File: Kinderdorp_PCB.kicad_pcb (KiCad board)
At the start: 2 copper layers, 39 parts, among them J1 Conn_01x08, Q1 2N7002_C306856, U2 AMS1117-3.3_C347222, U5 ESP32-C3-WROOM-02-N4(4MB)

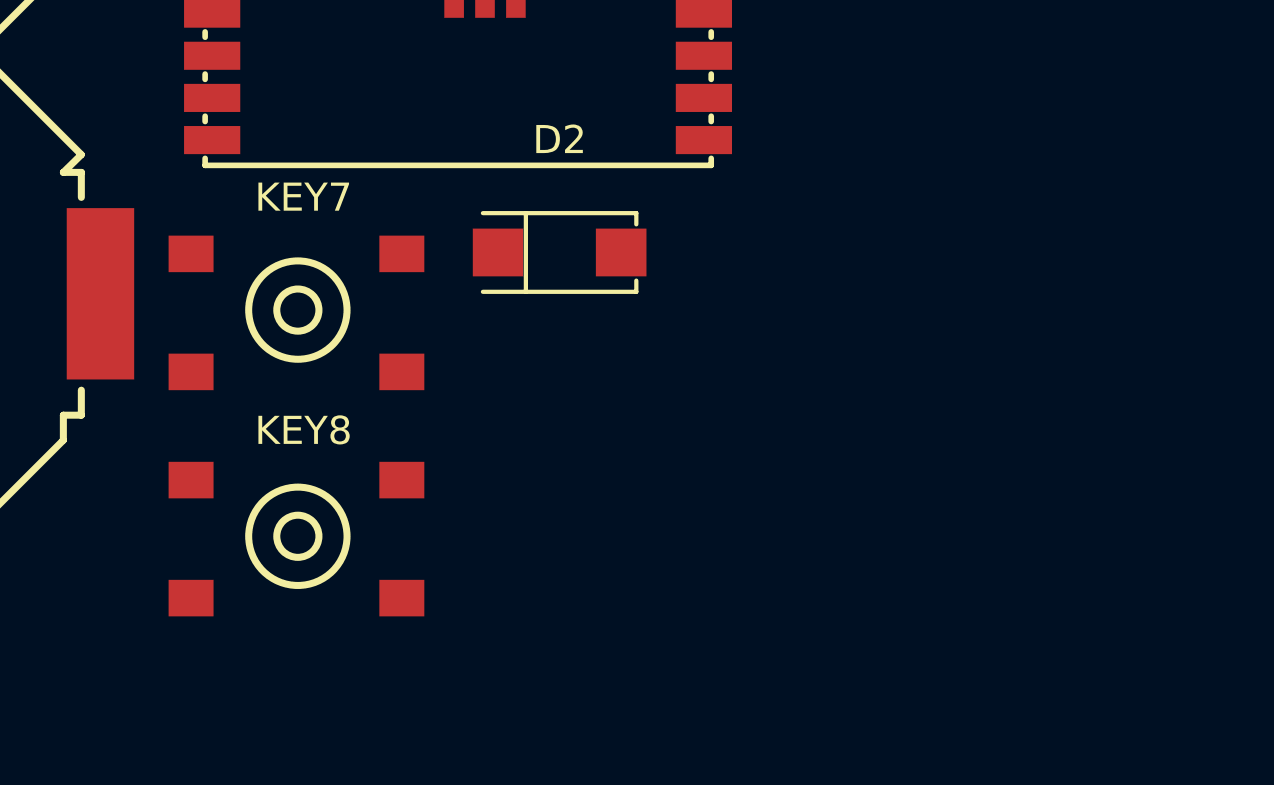
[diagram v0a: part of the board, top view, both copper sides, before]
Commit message: updated all 3d models
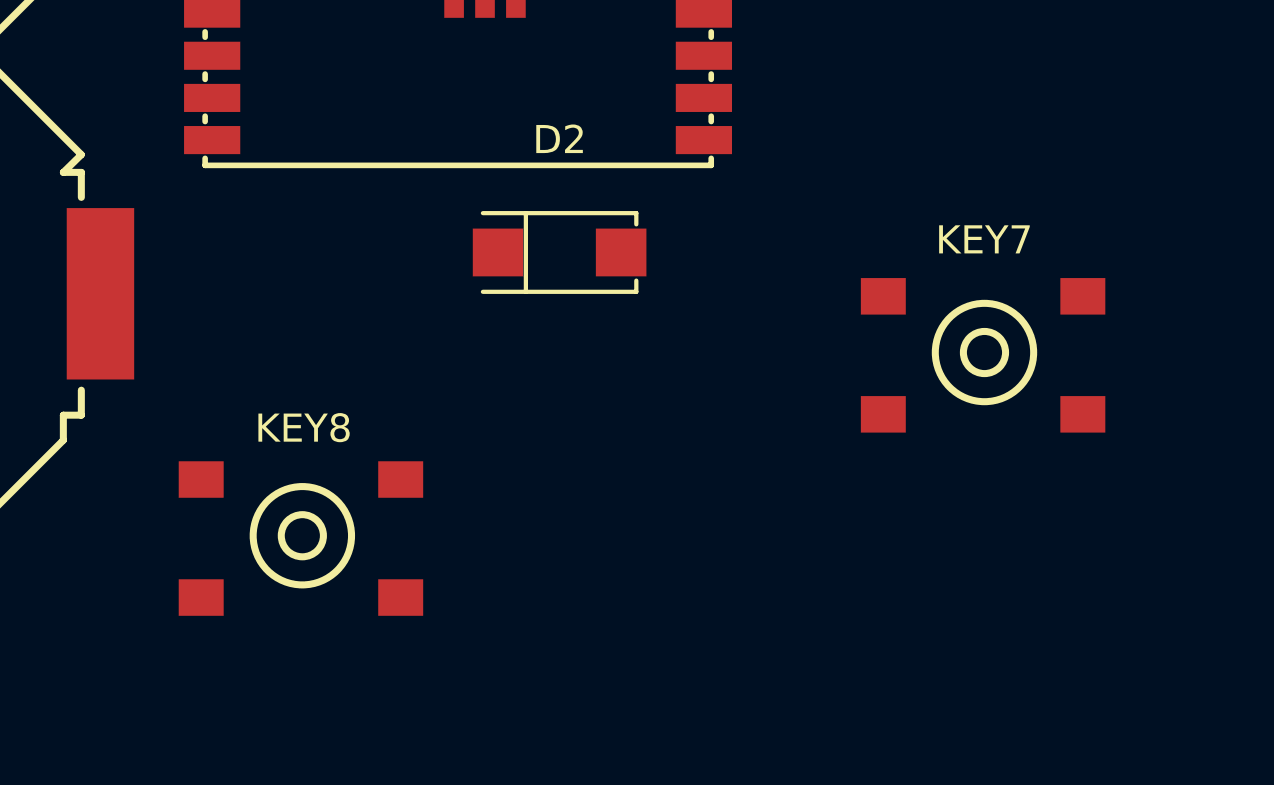
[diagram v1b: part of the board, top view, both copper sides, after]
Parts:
- moved KEY7 24.3 mm to (107.5, 84.6)
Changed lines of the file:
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@@
 		)
 		(embedded_fonts no)
-		(model "${EASYEDA2KICAD}/easyeda2kicad.3dshapes/LED-SMD_4P-L5.0-W5.0-BL_TC5050RGB.wrl"
+		(model "${KIPRJMOD}/packages3D/LED-SMD_4P-L5.0-W5.0-BL_TC5050RGB.step"
 			(offset
 				(xyz 0 -0 -0)
@@
 		(model "${KICAD9_3DMODEL_DIR}/OptoDevice.3dshapes/R_LDR_5.1x4.3mm_P3.4mm_Vertical.wrl"
 			(offset
-				(xyz 0 0 0)
+				(xyz 0 0 -2.2)
 			)
 			(scale
@@
 			)
 			(rotate
-				(xyz 0 0 0)
+				(xyz -0 -0 -0)
 			)
 		)
@@
 		)
 		(embedded_fonts no)
-		(model "${EASYEDA2KICAD}/easyeda2kicad.3dshapes/SOT-223-4P_L6.5-W3.5-H1.6-LS7.0-P2.30.wrl"
+		(model "${KIPRJMOD}/packages3D/SOT-223-4P_L6.5-W3.5-H1.6-LS7.0-P2.30.step"
 			(offset
-				(xyz -941.76 660.4 -0)
+				(xyz 0 0 -0)
 			)
 			(scale
@@
 			)
 			(rotate
-				(xyz 0 0 180)
+				(xyz -0 -0 180)
 			)
 		)
@@
 		)
 		(embedded_fonts no)
-		(model "${EASYEDA2KICAD}/easyeda2kicad.3dshapes/LED-SMD_4P-L5.0-W5.0-BL_TC5050RGB.wrl"
+		(model "${KIPRJMOD}/packages3D/LED-SMD_4P-L5.0-W5.0-BL_TC5050RGB.step"
 			(offset
 				(xyz 0 -0 -0)
@@
 		)
 		(embedded_fonts no)
-		(model "${EASYEDA2KICAD}/easyeda2kicad.3dshapes/LED-SMD_4P-L5.0-W5.0-BL_TC5050RGB.wrl"
+		(model "${KIPRJMOD}/packages3D/LED-SMD_4P-L5.0-W5.0-BL_TC5050RGB.step"
 			(offset
 				(xyz 0 -0 -0)
@@
 		)
 		(embedded_fonts no)
-		(model "${EASYEDA2KICAD}/easyeda2kicad.3dshapes/LED-SMD_4P-L5.0-W5.0-BL_TC5050RGB.wrl"
+		(model "${KIPRJMOD}/packages3D/LED-SMD_4P-L5.0-W5.0-BL_TC5050RGB.step"
 			(offset
 				(xyz 0 -0 -0)
@@
 	(footprint "easyeda2kicad:KEY-SMD_4P-L6.2-W6.2-P4.50-LS9.0"
 		(layer "F.Cu")
-		(at 83.225 83.08)
+		(at 107.45 84.6)
 		(property "Reference" "KEY7"
 			(at 0 -4 0)
@@
 			(at 0 6.25 0)
 			(layer "F.Fab")
+			(hide yes)
 			(effects
 				(font
@@
 		(attr smd)
 		(fp_circle
-			(center -0.2 0)
-			(end 0.55 0)
+			(center 0.01 -0.01)
+			(end 0.76 -0.01)
 			(stroke
 				(width 0.25)
@@
 		)
 		(fp_circle
-			(center -0.2 0)
-			(end 1.55 0)
+			(center 0.01 -0.01)
+			(end 1.76 -0.01)
 			(stroke
 				(width 0.25)
@@
 		)
 		(fp_rect
-			(start -5 -3.25)
-			(end 4.5 3.25)
+			(start -4.59 -2.93)
+			(end 4.51 3.07)
 			(stroke
 				(width 0.05)
@@
 		)
 		(fp_circle
-			(center -4.5 -2.85)
-			(end -4.47 -2.85)
+			(center -4.09 -2.86)
+			(end -4.06 -2.86)
 			(stroke
 				(width 0.06)
@@
 		)
 		(fp_text user "${REFERENCE}"
-			(at 0 0.25 0)
+			(at 0.41 0.24 0)
 			(layer "F.Fab")
 			(effects
@@
 		)
 		(pad "1" smd rect
-			(at -4 -2 180)
+			(at -3.59 -2.01 180)
 			(size 1.6 1.3)
 			(layers "F.Cu" "F.Mask" "F.Paste")
@@
 		)
 		(pad "2" smd rect
-			(at 3.5 -2 180)
+			(at -3.59 2.19 180)
 			(size 1.6 1.3)
 			(layers "F.Cu" "F.Mask" "F.Paste")
@@
 		)
 		(pad "3" smd rect
-			(at -4 2.2 180)
+			(at 3.51 -2.01 180)
 			(size 1.6 1.3)
 			(layers "F.Cu" "F.Mask" "F.Paste")
@@
 		)
 		(pad "4" smd rect
-			(at 3.5 2.2 180)
+			(at 3.51 2.19 180)
 			(size 1.6 1.3)
 			(layers "F.Cu" "F.Mask" "F.Paste")
@@
 		)
 		(embedded_fonts no)
-		(model "${EASYEDA2KICAD}/easyeda2kicad.3dshapes/KEY-SMD_4P-L6.2-W6.2-H5.0-LS9.0-P4.5.wrl"
+		(model "${KIPRJMOD}/packages3D/Tactile_SMD_5x5mm.STEP"
 			(offset
 				(xyz 0 -0 -0)
 			)
 			(scale
-				(xyz 1 1 1)
+				(xyz 1.1 1.1 1)
 			)
 			(rotate
-				(xyz 0 0 0)
+				(xyz -0 -0 -0)
 			)
 		)
@@
 		)
 		(embedded_fonts no)
-		(model "${EASYEDA2KICAD}/easyeda2kicad.3dshapes/LED-SMD_4P-L5.0-W5.0-BL_TC5050RGB.wrl"
+		(model "${KIPRJMOD}/packages3D/LED-SMD_4P-L5.0-W5.0-BL_TC5050RGB.step"
 			(offset
 				(xyz 0 -0 -0)
@@
 		)
 		(embedded_fonts no)
+		(model "${KIPRJMOD}/packages3D/Buzzer.STEP"
+			(offset
+				(xyz 0 0 0)
+			)
+			(scale
+				(xyz 1 1 1)
+			)
+			(rotate
+				(xyz -90 -0 -90)
+			)
+		)
 	)
 	(footprint "easyeda2kicad:SOT-23-3_L2.9-W1.3-P1.90-LS2.4-BR"
@@
 		)
 		(embedded_fonts no)
-		(model "${EASYEDA2KICAD}/easyeda2kicad.3dshapes/SOT-23-3P_L2.9-W1.3-H1.0-LS2.4-P0.95.wrl"
+		(model "${KIPRJMOD}/packages3D/SOT-23.step"
 			(offset
-				(xyz -861.57 843.28 -0)
+				(xyz 0 0 -0)
 			)
 			(scale
@@
 			)
 			(rotate
-				(xyz 0 0 180)
+				(xyz -0 -0 180)
 			)
 		)
@@
 		)
 		(embedded_fonts no)
-		(model "${EASYEDA2KICAD}/easyeda2kicad.3dshapes/BAT-SMD_MY-2032-12.wrl"
+		(model "${KICAD9_3RD_PARTY}/BAT-SMD_MY-2032-12.step"
 			(offset
 				(xyz 0 -0 -0)
@@
 		)
 		(embedded_fonts no)
-		(model "${EASYEDA2KICAD}/easyeda2kicad.3dshapes/TYPE-C-SMD_TYPE-C-6P_5.wrl"
+		(model "${KIPRJMOD}/packages3D/TYPE-C-SMD_TYPE-C-6P_5.step"
 			(offset
-				(xyz 0 -1.18 1)
+				(xyz 0 -1.18 0)
 			)
 			(scale
@@
 			)
 			(rotate
-				(xyz 0 0 0)
+				(xyz -0 -0 -0)
 			)
 		)
@@
 		)
 		(embedded_fonts no)
-		(model "${EASYEDA2KICAD}/easyeda2kicad.3dshapes/SMA_L4.4-W2.6-LS5.0-RD.wrl"
+		(model "${KIPRJMOD}/packages3D/SMA_L4.4-W2.6-LS5.0-RD.step"
 			(offset
 				(xyz 0 -0 -0)
@@
 		)
 		(embedded_fonts no)
-		(model "${EASYEDA2KICAD}/easyeda2kicad.3dshapes/LED-SMD_4P-L5.0-W5.0-BL_TC5050RGB.wrl"
+		(model "${KIPRJMOD}/packages3D/LED-SMD_4P-L5.0-W5.0-BL_TC5050RGB.step"
 			(offset
 				(xyz 0 -0 -0)
@@
 		)
 		(embedded_fonts no)
-		(model "${EASYEDA2KICAD}/easyeda2kicad.3dshapes/LED-SMD_4P-L5.0-W5.0-BL_TC5050RGB.wrl"
+		(model "${KIPRJMOD}/packages3D/LED-SMD_4P-L5.0-W5.0-BL_TC5050RGB.step"
 			(offset
 				(xyz 0 -0 -0)
@@
 		(at 83.225 91.13)
 		(property "Reference" "KEY8"
-			(at 0 -3.75 0)
+			(at 0 -3.83 0)
 			(layer "F.SilkS")
 			(effects
@@
 		)
 		(property "Value" "DTSM-61R-V-T/R"
-			(at 0 6.5 0)
+			(at 0.36 6.48 0)
 			(layer "F.Fab")
 			(effects
@@
 		(attr smd)
 		(fp_circle
-			(center -0.2 0)
-			(end 0.55 0)
+			(center -0.04 -0.02)
+			(end 0.71 -0.02)
 			(stroke
 				(width 0.25)
@@
 		)
 		(fp_circle
-			(center -0.2 0)
-			(end 1.55 0)
+			(center -0.04 -0.02)
+			(end 1.71 -0.02)
 			(stroke
 				(width 0.25)
@@
 		)
 		(fp_rect
-			(start -5 -3.25)
-			(end 4.5 3.25)
+			(start -4.64 -2.94)
+			(end 4.46 3.06)
 			(stroke
 				(width 0.05)
@@
 		)
 		(fp_circle
-			(center -4.5 -2.85)
-			(end -4.47 -2.85)
+			(center -4.14 -2.87)
+			(end -4.11 -2.87)
 			(stroke
 				(width 0.06)
@@
 		)
 		(fp_text user "${REFERENCE}"
-			(at 0 0.25 0)
+			(at 0.36 0.23 0)
 			(layer "F.Fab")
 			(effects
@@
 		)
 		(pad "1" smd rect
-			(at -4 -2 180)
+			(at -3.64 -2.02 180)
 			(size 1.6 1.3)
 			(layers "F.Cu" "F.Mask" "F.Paste")
@@
 		)
 		(pad "2" smd rect
-			(at 3.5 -2 180)
+			(at -3.64 2.18 180)
 			(size 1.6 1.3)
 			(layers "F.Cu" "F.Mask" "F.Paste")
@@
 		)
 		(pad "3" smd rect
-			(at -4 2.2 180)
+			(at 3.46 -2.02 180)
 			(size 1.6 1.3)
 			(layers "F.Cu" "F.Mask" "F.Paste")
@@
 		)
 		(pad "4" smd rect
-			(at 3.5 2.2 180)
+			(at 3.46 2.18 180)
 			(size 1.6 1.3)
 			(layers "F.Cu" "F.Mask" "F.Paste")
@@
 		)
 		(embedded_fonts no)
-		(model "${EASYEDA2KICAD}/easyeda2kicad.3dshapes/KEY-SMD_4P-L6.2-W6.2-H5.0-LS9.0-P4.5.wrl"
+		(model "${KIPRJMOD}/packages3D/Tactile_SMD_5x5mm.STEP"
 			(offset
 				(xyz 0 -0 -0)
 			)
 			(scale
-				(xyz 1 1 1)
+				(xyz 1.1 1.1 1)
 			)
 			(rotate
-				(xyz 0 0 0)
+				(xyz -0 -0 -0)
 			)
 		)
@@
 		)
 		(embedded_fonts no)
-		(model "${EASYEDA2KICAD}/easyeda2kicad.3dshapes/BAT-SMD_MY-2032-12.wrl"
+		(model "${KICAD9_3RD_PARTY}/BAT-SMD_MY-2032-12.step"
 			(offset
 				(xyz 0 -0 -0)
@@
 		)
 		(embedded_fonts no)
-		(model "${EASYEDA2KICAD}/easyeda2kicad.3dshapes/BULETM-SMD_ESPRESSIF_ESP32-C3-WROOM-02-N4-4MB.wrl"
+		(model "${KIPRJMOD}/packages3D/BULETM-SMD_ESPRESSIF_ESP32-C3-WROOM-02-N4-4MB.step"
 			(offset
 				(xyz -0 3.1 -0)
@@
 		)
 		(embedded_fonts no)
-		(model "${EASYEDA2KICAD}/easyeda2kicad.3dshapes/LED-SMD_4P-L5.0-W5.0-BL_TC5050RGB.wrl"
+		(model "${KIPRJMOD}/packages3D/LED-SMD_4P-L5.0-W5.0-BL_TC5050RGB.step"
 			(offset
 				(xyz 0 -0 -0)

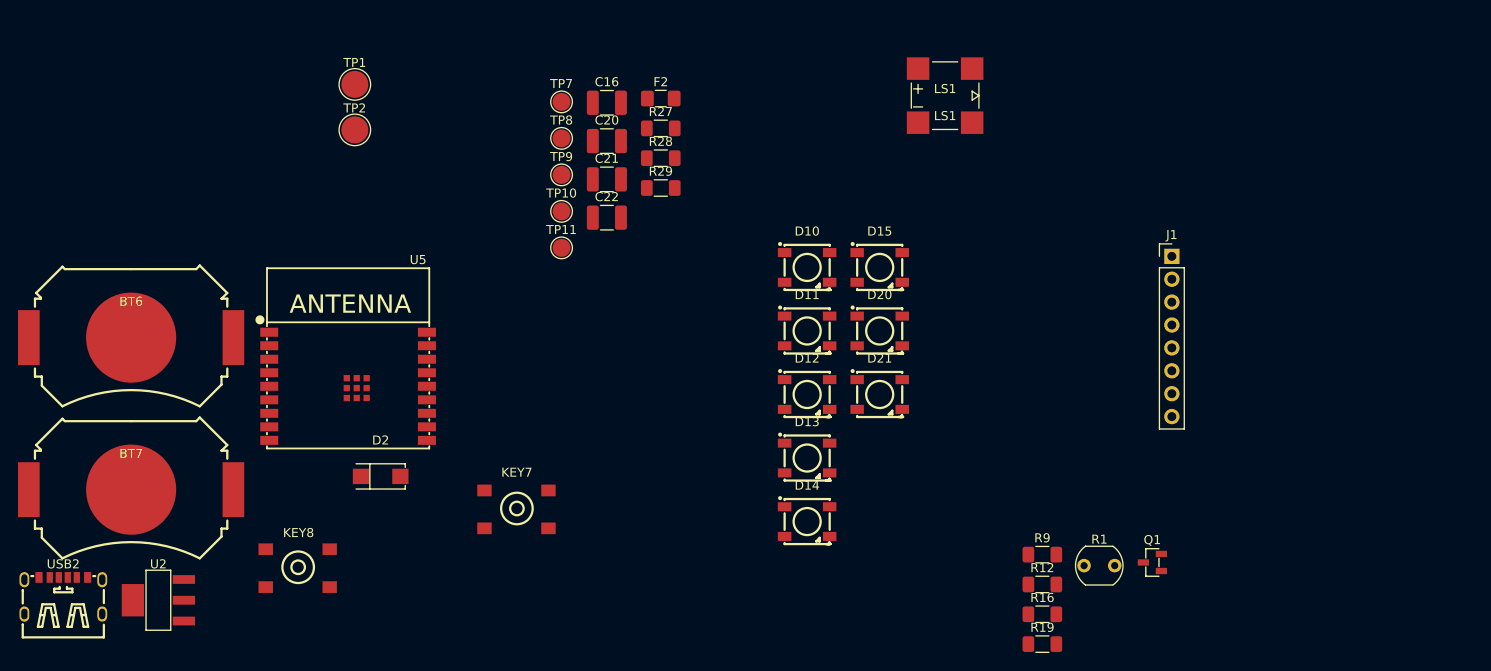
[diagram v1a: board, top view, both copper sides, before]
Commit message: added AAA box 3d model and reference images
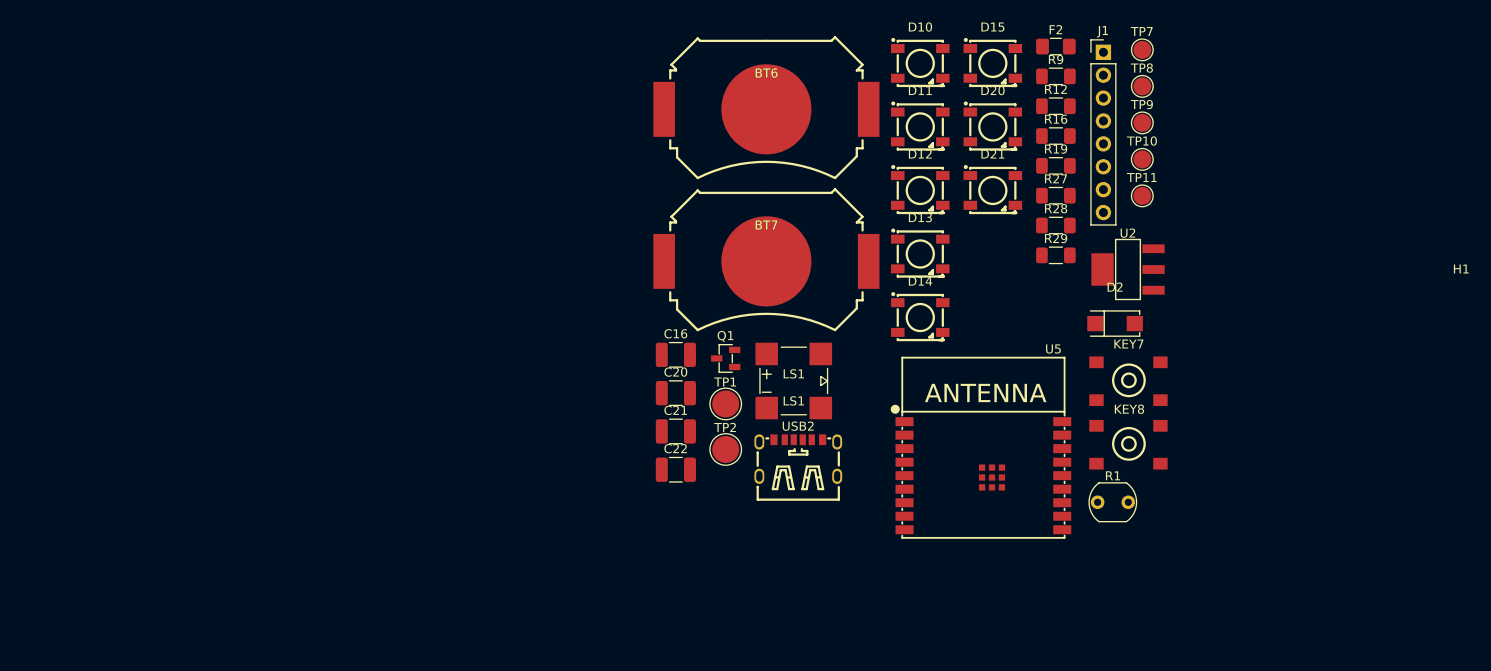
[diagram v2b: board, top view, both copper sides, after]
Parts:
- added H1: Batteryplaceholder, MountingHole:MountingHole_2.1mm, F.Cu at (212.2, 61.1)
- moved U2 113.7 mm to (175.3, 58.1)
- moved KEY8 93.2 mm to (175.4, 77.4)
- moved D2 83.2 mm to (173.8, 64.1)
- moved USB2 83.0 mm to (138.7, 79.0)
- moved BT6 74.9 mm to (135.1, 40.3)
- moved BT7 74.9 mm to (135.1, 57.2)
- moved U5 71.2 mm to (159.2, 81.0)
- moved KEY7 69.4 mm to (175.4, 70.4)
- moved TP10 64.7 mm to (176.9, 45.9)
- moved TP11 64.7 mm to (176.9, 49.9)
- moved TP7 64.7 mm to (176.9, 33.7)
- moved TP8 64.7 mm to (176.9, 37.8)
- moved TP9 64.7 mm to (176.9, 41.8)
- moved TP2 54.3 mm to (130.6, 78.0)
- moved TP1 54.3 mm to (130.6, 73.0)
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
